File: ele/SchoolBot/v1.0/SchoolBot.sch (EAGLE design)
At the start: 62 parts, among them X1 M8, X2 M8, X4 POWER_IN

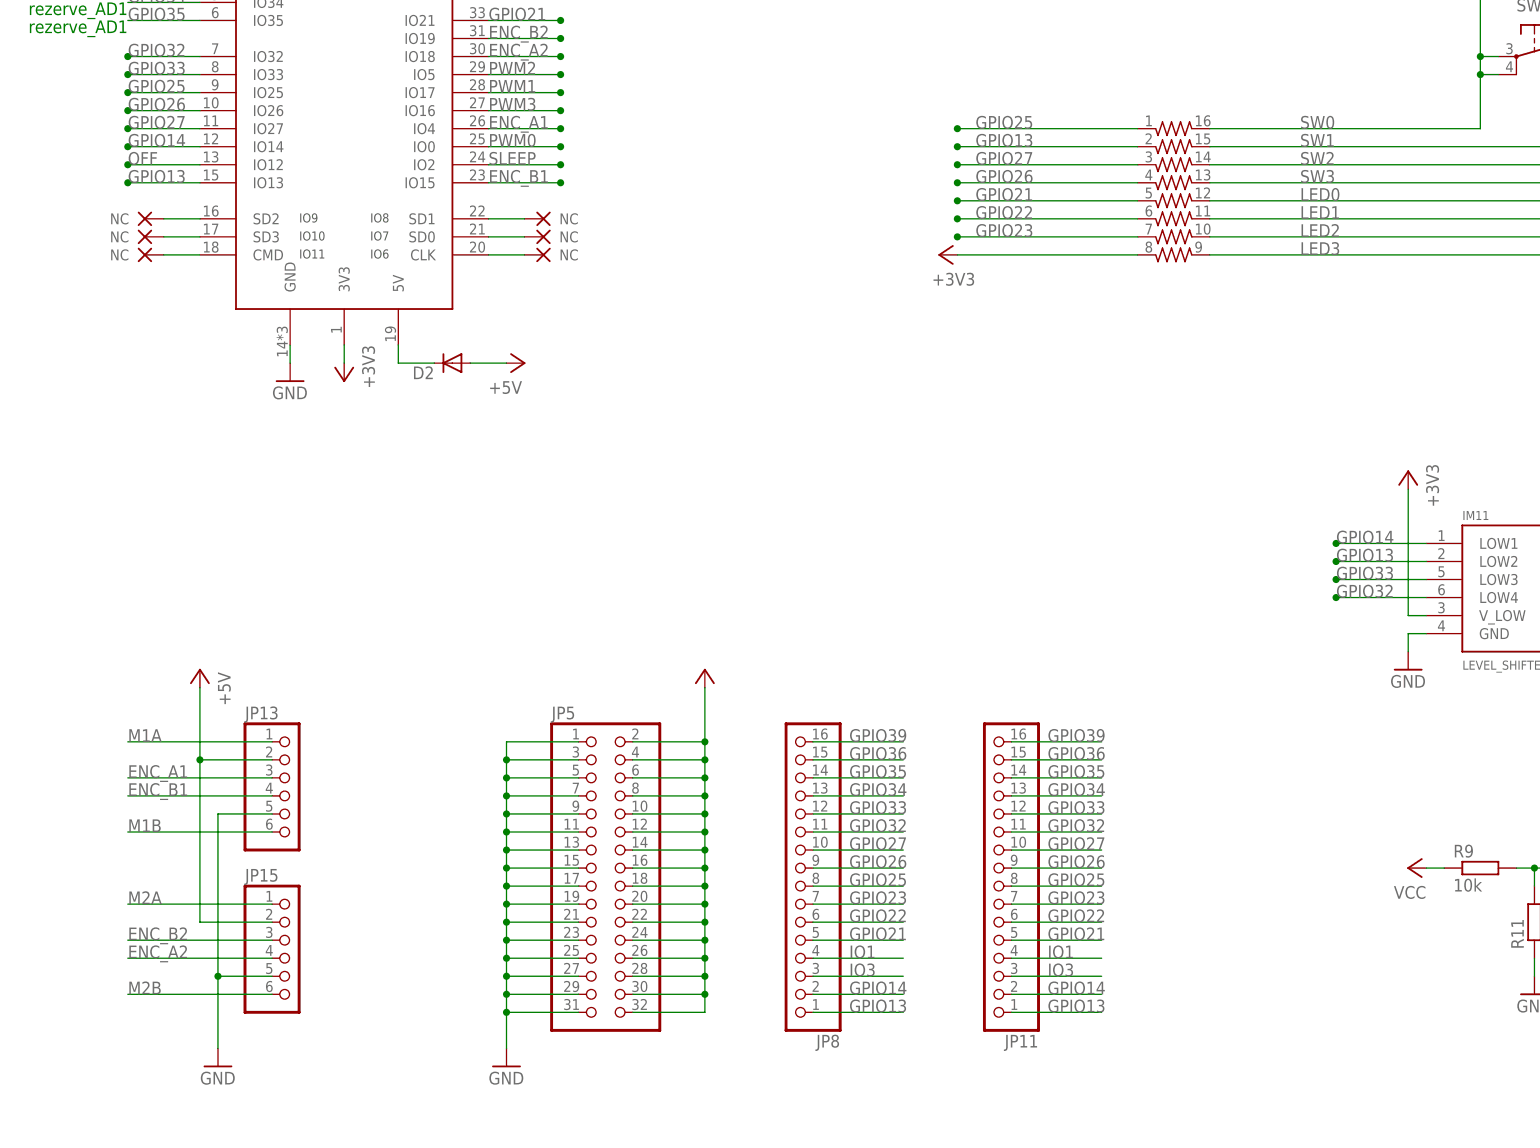
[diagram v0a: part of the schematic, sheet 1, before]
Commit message: off pin
presun vypinani desky na pin 13 kvuli nahrav8ni programu
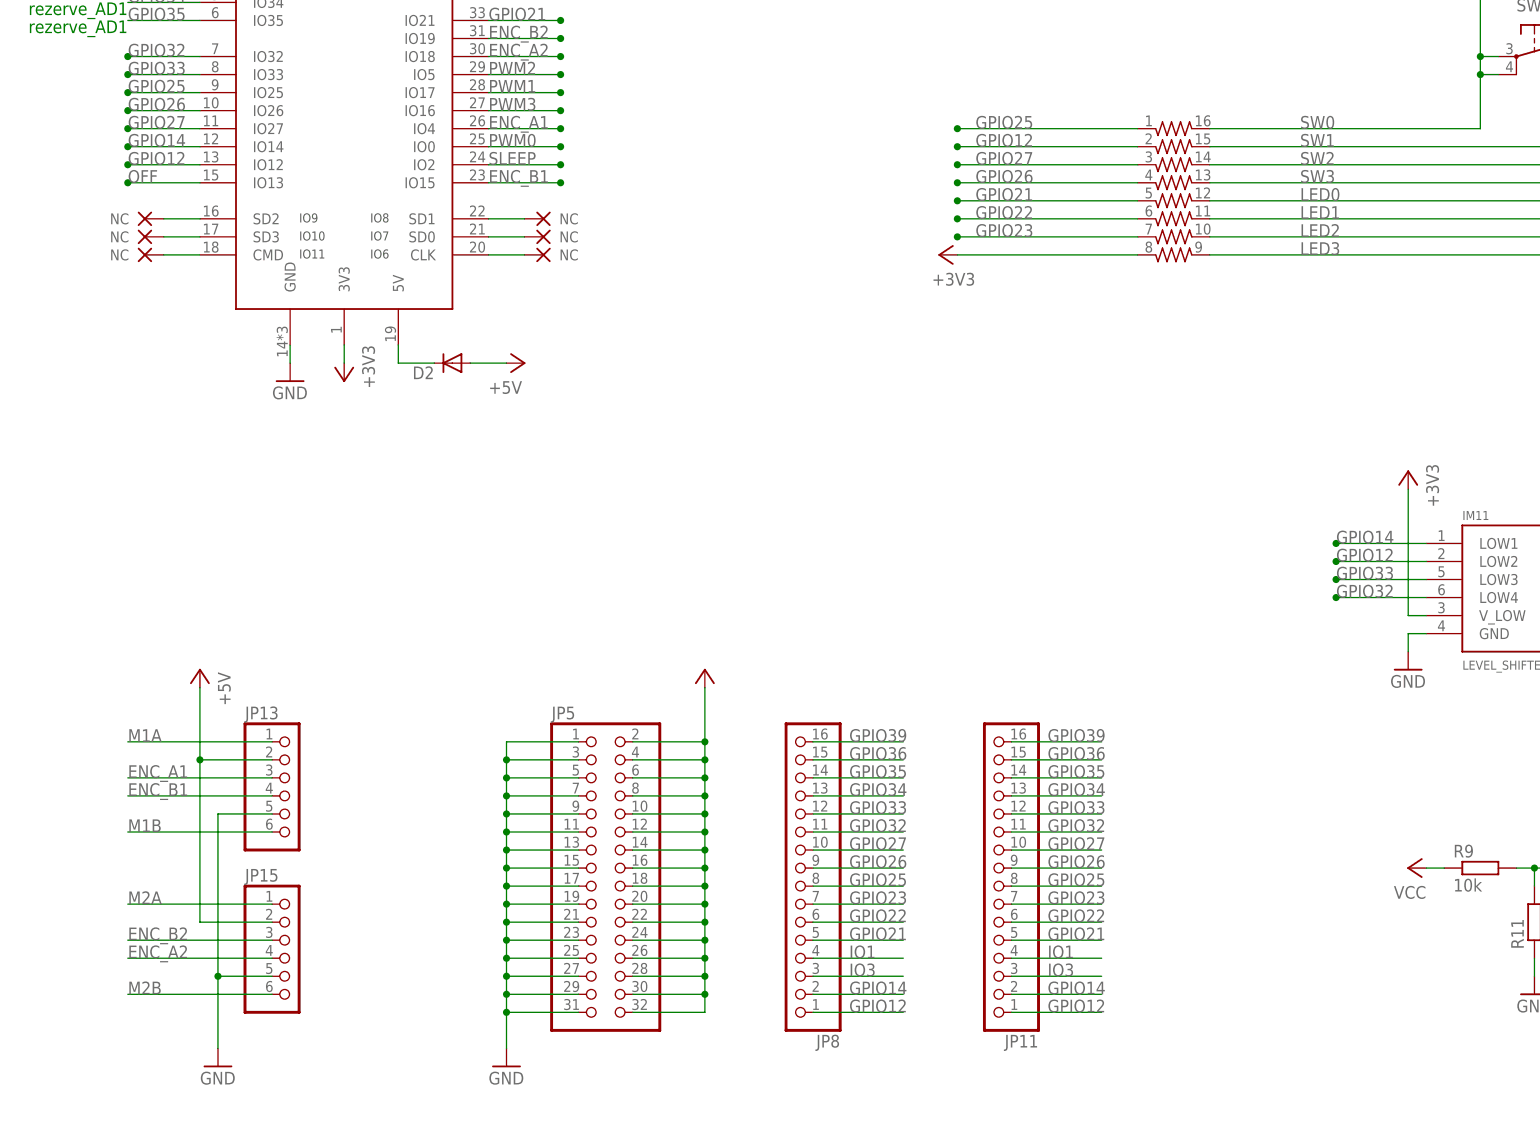
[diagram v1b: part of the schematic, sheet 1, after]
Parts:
- R2: device rcl_upravena:R-EU_0204/2V -> rcl_upravena:R-EU_0204/5
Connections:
- removed net GPIO13: IM11.LOW2, IM6.IO13, JP11.1, JP8.1, RN1B.1
- new net GPIO12: IM11.LOW2, IM6.IO12, JP11.1, JP8.1, RN1B.1
- net OFF: now also IM6.IO13; no longer IM6.IO12

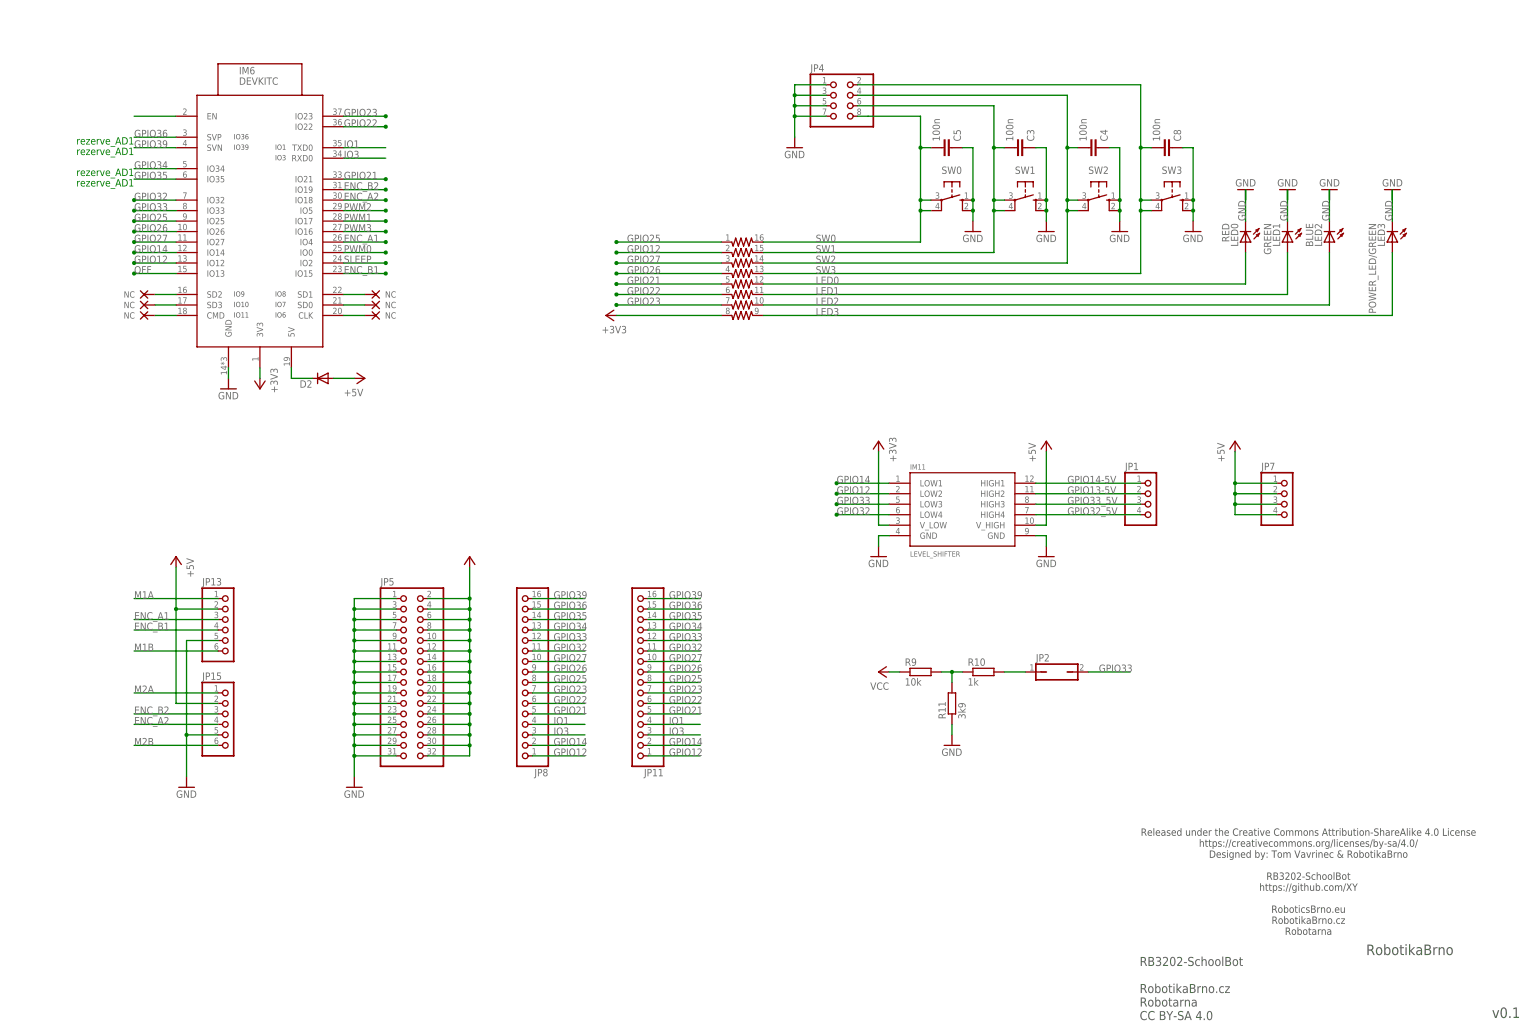
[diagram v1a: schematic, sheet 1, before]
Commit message: program ovladani serv
zatim jen s lehce upravenym RBControl
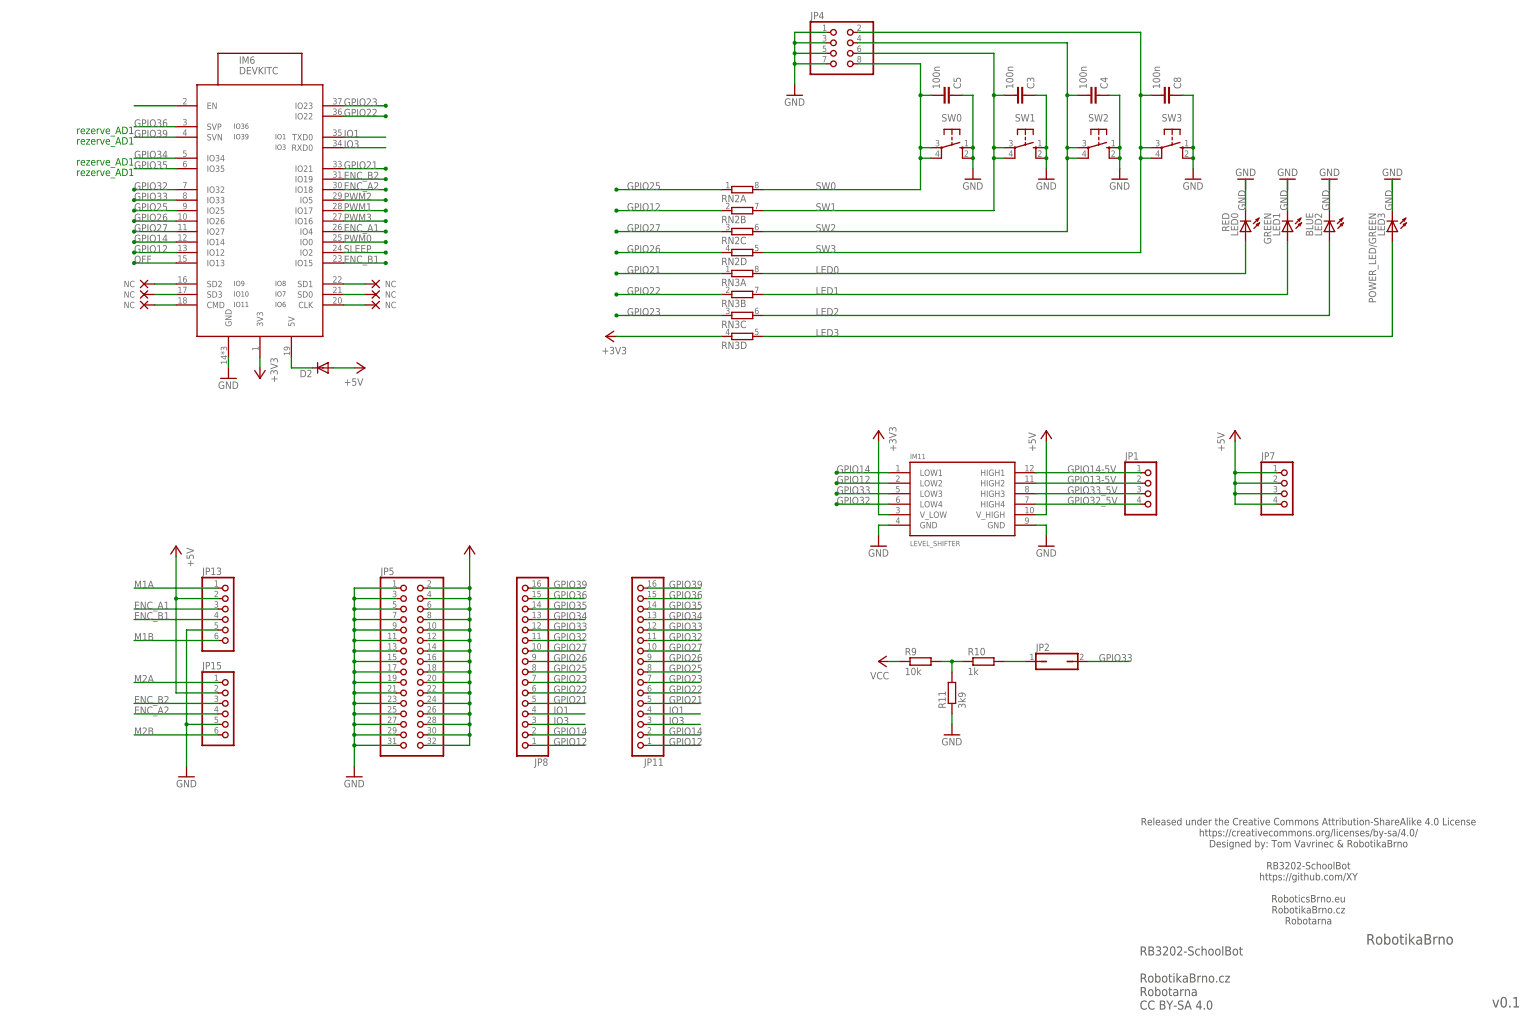
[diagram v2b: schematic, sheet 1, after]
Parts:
- removed RN1: (no value), resistor-array:741-16_SNS
- added RN2, RN3: (no value), resistor-dil:4R-NEXBS8V
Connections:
- net +3V3: now also RN3D.1; no longer RN1H.1
- net GPIO12: now also RN2B.1; no longer RN1B.1
- net GPIO21: now also RN3A.1; no longer RN1E.1
- net GPIO22: now also RN3B.1; no longer RN1F.1
- net GPIO23: now also RN3C.1; no longer RN1G.1
- net GPIO25: now also RN2A.1; no longer RN1A.1
- net GPIO26: now also RN2D.1; no longer RN1D.1
- net GPIO27: now also RN2C.1; no longer RN1C.1
- net LED0: now also RN3A.2; no longer RN1E.2
- net LED1: now also RN3B.2; no longer RN1F.2
- net LED2: now also RN3C.2; no longer RN1G.2
- net LED3: now also RN3D.2; no longer RN1H.2
- net SW0: now also RN2A.2; no longer RN1A.2
- net SW1: now also RN2B.2; no longer RN1B.2
- net SW2: now also RN2C.2; no longer RN1C.2
- net SW3: now also RN2D.2; no longer RN1D.2
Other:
- moved on the sheet: C3, C4, C5, C8, D2, IM11, IM6, JP1, JP11, JP13, JP15, JP2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

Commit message: new board
-komplenti prekreslini desky
-doplneni rady pinhedu gnd pro 5v piniste
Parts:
- JP1: device pinhead:PINHD-1X4 -> pinhead:PINHD-2X4
- JP7: device pinhead:PINHD-1X4/90 -> pinhead:PINHD-1X4
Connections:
- net GND: now also JP1.2, JP1.4, JP1.6, JP1.8
- net GPIO13-5V: now also JP1.3; no longer JP1.2
- net GPIO32_5V: now also JP1.7; no longer JP1.4
- net GPIO33_5V: now also JP1.5; no longer JP1.3

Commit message: nove rozlozeni
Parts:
- removed J2: (no value), jumper:JP2E
- removed JP13, JP15: (no value), pinhead:PINHD-1X6
- removed JP14: (no value), pinhead:PINHD-1X3
- added JP16: (no value), pinhead:PINHD-2X4
- added JP42, JP47, JP48: 292161-3, iServo_connector:292161-3
- added JP9: (no value), pinhead:PINHD-2X5
- added R8: 10k, rcl_upravena:R-EU_R0805
- JP3: value START_BUTTON -> (none); device pinhead:PINHD-1X2 -> pinhead:PINHD-1X4
- JP4: device pinhead:PINHD-2X4 -> pinhead:PINHD-2X3
- JP6: value STOP_BUTTON -> (none); device pinhead:PINHD-1X2 -> pinhead:PINHD-2X4
- R2: device rcl_upravena:R-EU_0204/5 -> rcl_upravena:R-EU_R0805
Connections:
- net BAT_PROT1 renamed BAT_POL+
- removed net N$3: J2.2, JP14.2
- removed net START_BUTTON1: C1.2, JP3.1, R4.2, SW4.P, SW4.P1
- new net EN: JP16.4, R8.1
- new net N$5: JP9.10, JP9.2, JP9.4, JP9.6, JP9.8
- new net N$7: C1.2, JP16.6, R4.2, SW4.P, SW4.P1
- net +3V3: now also R8.2
- net +5V: now also JP1.2, JP1.4, JP1.6, JP1.8, JP16.2, JP6.1, JP6.2; no longer JP13.2, JP15.2, JP7.1, JP7.2, JP7.3, JP7.4
- net ENC_A1: now also JP6.6; no longer JP13.3
- net ENC_A2: now also JP6.3; no longer JP15.4
- net ENC_B1: now also JP6.4; no longer JP13.4
- net ENC_B2: now also JP6.5; no longer JP15.3
- net GND: now also JP16.1, JP16.3, JP16.5, JP16.7, JP42.1, JP47.1, JP48.1, JP6.7, JP6.8, JP7.1, JP7.2, JP7.3, JP7.4; no longer JP1.2, JP1.4, JP1.6, JP1.8, JP13.5, JP14.1, JP15.5, JP3.2, JP4.7, JP6.2
- net GPIO13-5V: now also JP3.2
- net GPIO14-5V: now also JP3.1
- net GPIO23: now also JP42.3, JP47.3, JP48.3; no longer JP14.3
- net GPIO32_5V: now also JP3.4
- net GPIO33_5V: now also JP3.3
- net LED0: now also JP9.1
- net LED1: now also JP9.3
- net LED2: now also JP9.5
- net LED3: now also JP9.7
- net M1A: now also X1-1.KL; no longer JP13.1, X1-2.KL
- net M1B: now also X1-2.KL; no longer JP13.6, X1-1.KL
- net M2A: no longer JP15.1
- net M2B: no longer JP15.6
- net OFF: now also JP16.8; no longer JP6.1
- net SERVO_STEPDOWN_5V: no longer J2.3
- net SW0: now also JP4.6; no longer JP4.8
- net SW1: now also JP4.4; no longer JP4.6
- net SW2: now also JP4.2; no longer JP4.4
- net SW3: now also JP9.9; no longer JP4.2
- net VCC: now also JP42.2, JP47.2, JP48.2; no longer J2.1
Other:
- moved on the sheet: C2, D2, IM6, Q2, Q6, R1, R2, SW4, SW5, X1-1, X1-2

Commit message: new_board
nesting noveho rozlozeni
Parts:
- removed JP12: (no value), pinhead:PINHD-1X3
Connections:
- net N$7 renamed ON
- removed net N$5: JP9.10, JP9.2, JP9.4, JP9.6, JP9.8
- removed net N$6: IM6.EN
- net +5V: no longer JP1.2, JP1.4, JP1.6, JP1.8
- net EN: now also IM6.EN
- net ENC_B1: now also IM6.IO19; no longer IM6.IO15
- net ENC_B2: now also IM6.IO15; no longer IM6.IO19
- net GND: now also JP9.10, JP9.2, JP9.4, JP9.6, JP9.8; no longer JP12.1
- net GPIO12: now also IM11.LOW4, JP11.6, JP8.6; no longer IM11.LOW2, JP11.1, JP8.1
- net GPIO14: now also IM11.LOW3, JP11.7, JP8.7; no longer IM11.LOW1, JP11.2, JP8.2
- net GPIO14-5V: no longer JP12.3
- net GPIO22: now also JP11.2, JP8.2; no longer JP11.6, JP8.6
- net GPIO23: now also JP11.1, JP8.1; no longer JP11.7, JP8.7
- net GPIO25: now also JP11.10, JP8.10; no longer JP11.8, JP8.8
- net GPIO27: now also JP11.8, JP8.8; no longer JP11.10, JP8.10
- net GPIO32: now also IM11.LOW1, JP11.12, JP8.12; no longer IM11.LOW4, JP11.11, JP8.11
- net GPIO33: now also IM11.LOW2, JP11.11, JP8.11; no longer IM11.LOW3, JP11.12, JP8.12
- net GPIO34: now also JP11.14, JP8.14; no longer JP11.13, JP8.13
- net GPIO35: now also JP11.13, JP8.13; no longer JP11.14, JP8.14
- net GPIO36: now also JP11.16, JP8.16; no longer JP11.15, JP8.15
- net GPIO39: now also JP11.15, JP8.15; no longer JP11.16, JP8.16
- net SERVO_STEPDOWN_5V: now also JP1.2, JP1.4, JP1.6, JP1.8; no longer JP12.2
